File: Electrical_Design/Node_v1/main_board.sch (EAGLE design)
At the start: 23 parts, among them IC1 TP4056, IC2 REG1117

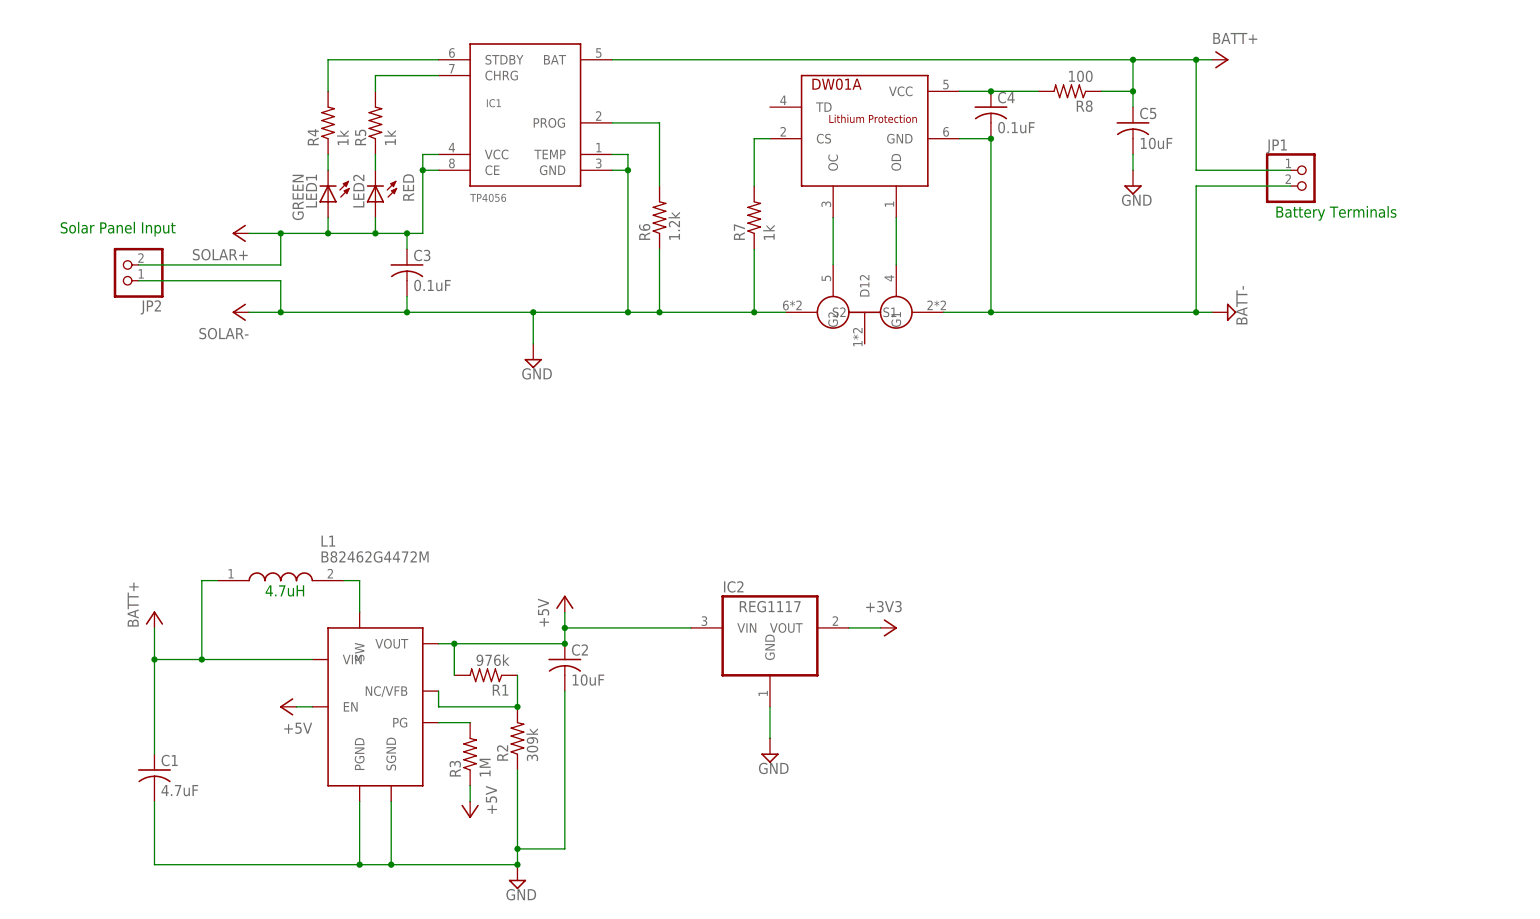
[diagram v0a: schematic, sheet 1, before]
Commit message: Adds current sensor to power page -- Adds microcontroller page
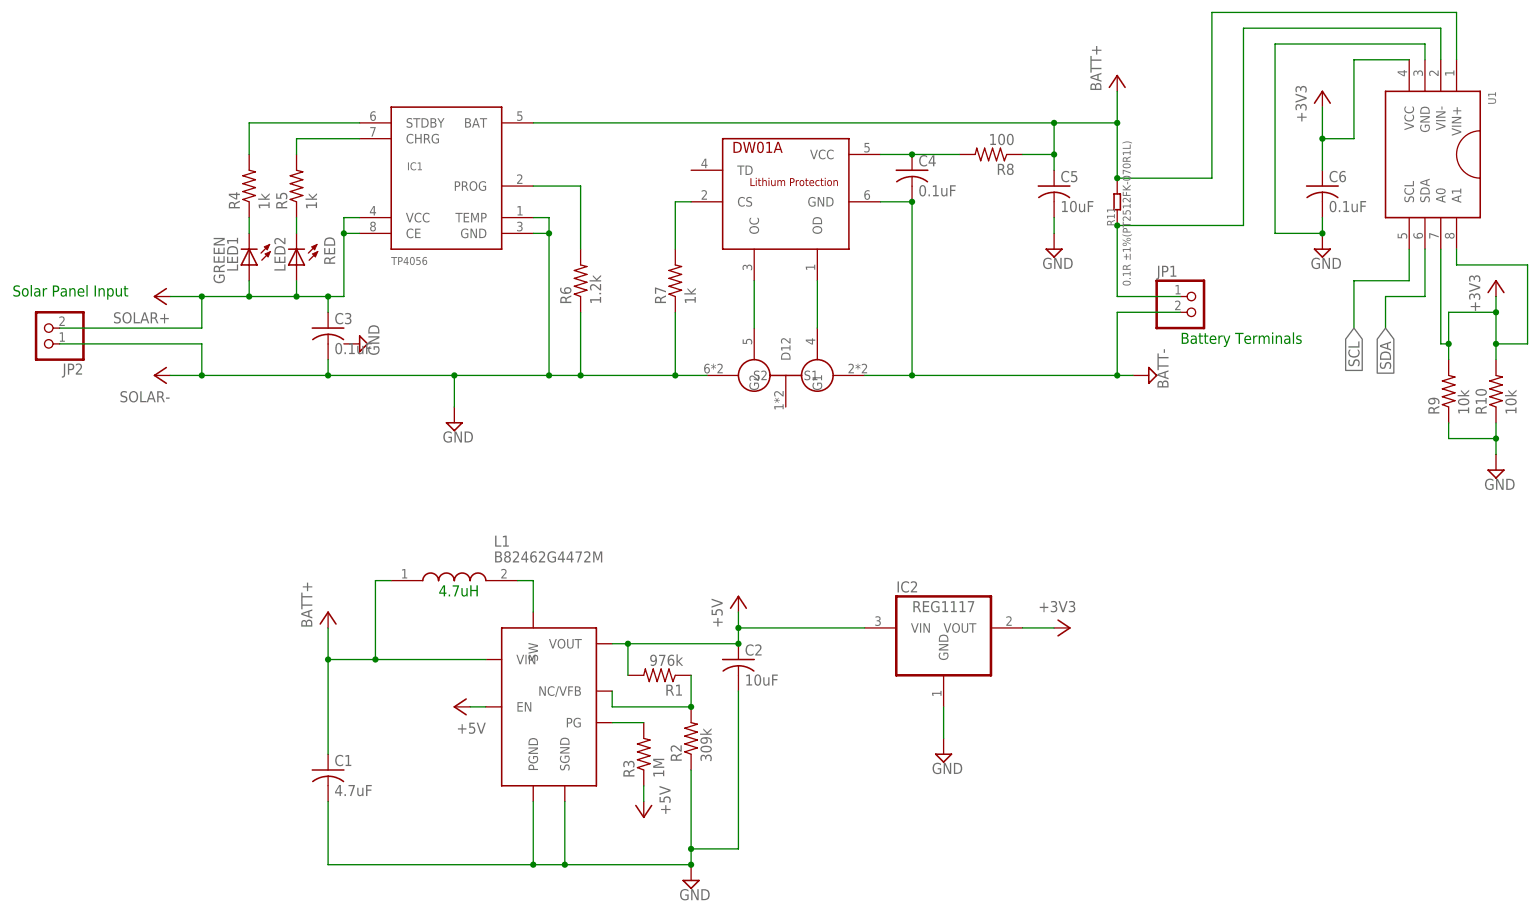
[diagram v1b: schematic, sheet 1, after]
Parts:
- added C6: 0.1uF, adafruit:C-USC1206
- added JP3: (no value), pinhead:PINHD-1X8
- added JP4, JP5: (no value), pinhead:PINHD-1X3
- added JP6: (no value), pinhead:PINHD-1X6
- added R10, R14, R9: 10k, adafruit:R-US_R1206
- added R11: 0.1R ±1%(PT2512FK-070R1L), RCL_INA219:R-2512
- added R12, R13, R15, R16: 4.7k, adafruit:R-US_R1206
- added S3, S4: 222AMVAAR, SamacSys_Parts:222AMVAAR
- added U1: (no value), IC_INA219:INA219
- added U2: ESP-WROOM-32, SparkFun-RF_ESP:ESP-WROOM-32
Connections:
- new net N$13: JP1.1, R11.1, U1.VIN-
- new net N$14: JP3.8, U2.IO5
- new net N$15: JP3.7, U2.IO23
- new net N$16: JP3.6, U2.IO19
- new net N$17: JP3.5, U2.IO18
- new net N$18: JP6.5, R14.1, S3.NO_1, S3.NO_2, U2.EN
- new net N$19: JP6.2, U2.TXD
- new net N$20: JP6.3, U2.RXD
- new net N$21: JP5.2, U2.SENSOR_VN
- new net N$22: JP6.6, S4.NO_1, S4.NO_2, U2.IO0
- new net N$23: JP4.2, R15.1
- new net N$24: R15.2, R16.2, U2.IO34
- new net SCL: JP3.1, R13.1, U1.SCL, U2.IO22
- new net SDA: JP3.2, R12.1, U1.SDA, U2.IO21
- net +3V3: now also C6.1, JP3.3, JP5.1, R10.2, R12.2, R13.2, R14.2, R9.2, U1.A0, U1.A1, U1.VCC, U2.3V3
- net +5V: now also JP4.1, JP6.1
- net BATT+: now also R11.2, U1.VIN+; no longer JP1.1
- net GND: now also C6.2, JP3.4, JP4.3, JP5.3, JP6.4, R10.1, R16.1, R9.1, S3.COM_1, S3.COM_2, S4.COM_1, S4.COM_2, U1.GND, U2.GND, U2.GND@1, U2.GND@15, U2.GND@38
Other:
- note added: "5V-IN"
- note added: "BOOT Button"
- note added: "CS"
- note added: "Camera"
- note added: "EN"
- note added: "EN Button"
- note added: "GND"
- note added: "IO0 (BOOT)"
- note added: "MISO"
- note added: "MOSI"
- note added: "RX"
- note added: "SCK"
- note added: "SCL"
- note added: "SDA"
- note added: "TX"
- note added: "VCC"
- note added: "Wind Direction"
- note added: "Wind Speed"
- moved on the sheet: C1, C2, C3, C4, C5, IC1, IC2, JP1, JP2, L1, LED1, LED2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

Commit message: Completes schematic layout
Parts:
- added C10: 0.22uF, adafruit:C-USC1206
- added C7, C8: 0.1uF, adafruit:C-USC1206
- added C9: 4.7uF, adafruit:C-USC1206
- added IC3: DS18B20U+, SamacSys_Parts:DS18B20U+
- added JP7: (no value), pinhead:PINHD-1X7
- added R17, R18, R21: 4.7k, adafruit:R-US_R1206
- added R19, R20, R22, R23: 10k, adafruit:R-US_R1206
- added TP1, TP10, TP11, TP12, TP13, TP14, TP15, TP16, TP17, TP18, TP19, TP2, TP20, TP21, TP22, TP23, TP24, TP25, TP26, TP27, TP28, TP29, TP3, TP30, TP4, TP5, TP6, TP7, TP8, TP9: TPPAD1-13, testpad:TPPAD1-13
- added U$4: SPARKFUN_HMC5883LSMD, SparkFun_HMC5883L_Breakout_v12:SPARKFUN_HMC5883LSMD
- added U3: BME280, BME280ComponentLibrary:BME280
- added U4: CCS811, CCS811_Breakout_Temp:CCS811
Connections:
- new net GND1: JP7.4
- new net GPIO17: IC3.DQ, R21.1, U2.IO17
- new net N$25: R17.1, U3.!CS
- new net N$26: R19.1, U4.!RESET!
- new net N$27: C10.1, U$4.SETP
- new net N$28: C10.2, U$4.SETC
- new net N$29: R22.2, U4.!WAKE!
- new net N$30: C9.1, U$4.C1
- new net N$31: TP1.TP, U4.SENSE
- new net N$32: TP2.TP, U4.PWM
- new net N$33: TP3.TP, U4.!INT!
- new net N$34: TP4.TP, U4.AUX
- new net N$35: TP5.TP, U$4.DRDY
- new net N$36: TP7.TP, U$1.TD
- new net N$37: TP6.TP, U$2.D12
- new net N$38: TP28.TP, U2.IO2
- new net N$39: TP27.TP, U2.IO4
- new net N$40: TP26.TP, U2.IO12
- new net N$41: TP25.TP, U2.IO13
- new net N$42: TP24.TP, U2.IO14
- new net N$43: TP23.TP, U2.IO15
- new net N$44: TP22.TP, U2.IO16
- new net N$45: TP21.TP, U2.IO20
- new net N$46: TP20.TP, U2.IO25
- new net N$47: TP19.TP, U2.IO26
- new net N$48: TP18.TP, U2.IO27
- new net N$49: TP17.TP, U2.IO32
- new net N$50: TP16.TP, U2.IO33
- new net N$51: TP15.TP, U2.IO35
- new net N$52: TP14.TP, U2.SHD
- new net N$53: TP13.TP, U2.SWP
- new net N$54: TP12.TP, U2.SCS
- new net N$55: TP11.TP, U2.SCK
- new net N$56: TP10.TP, U2.SDO
- new net N$57: TP9.TP, U2.SDI
- new net N$58: TP8.TP, U2.SENSOR_VP
- new net VCC: JP7.1, JP7.2, JP7.3
- net +3V3: now also C7.1, C8.1, IC3.VDD, JP7.6, R17.2, R18.1, R19.2, R20.1, R21.2, R23.1, U$4.S1, U$4.VDD, U$4.VDDIO, U3.VDD, U3.VDDIO, U4.VDD
- net +5V: now also JP7.5
- net GND: now also C7.2, C8.2, C9.2, IC3.GND, JP7.7, R18.2, R20.2, R22.1, U$4.GND@1, U$4.GND@2, U3.GND1, U3.GND2, U3.SDO/ADR, U4.ADDR, U4.GND
- net N$22: now also R23.2
- net SCL: now also TP29.TP, U$4.SCL, U3.SCK/SCL, U4.SCL
- net SDA: now also TP30.TP, U$4.SDA, U3.SDI/SDA, U4.SDA
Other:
- note added: "Optional - I2C Address Selector"
- note added: "Power Test Point"
- moved on the sheet: JP3, JP4, JP5, JP6, R12, R13, R14, R15, R16, S3, S4, U2

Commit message: Begins main board layout
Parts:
- added JP8, JP9: (no value), pinhead:PINHD-1X5
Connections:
- net +3V3: now also JP8.2, JP9.2
- net GND: now also JP8.1, JP9.1
- net GPIO17: now also JP8.5, JP9.5
- net SCL: now also JP8.4, JP9.4
- net SDA: now also JP8.3, JP9.3
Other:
- moved on the sheet: IC3, R21

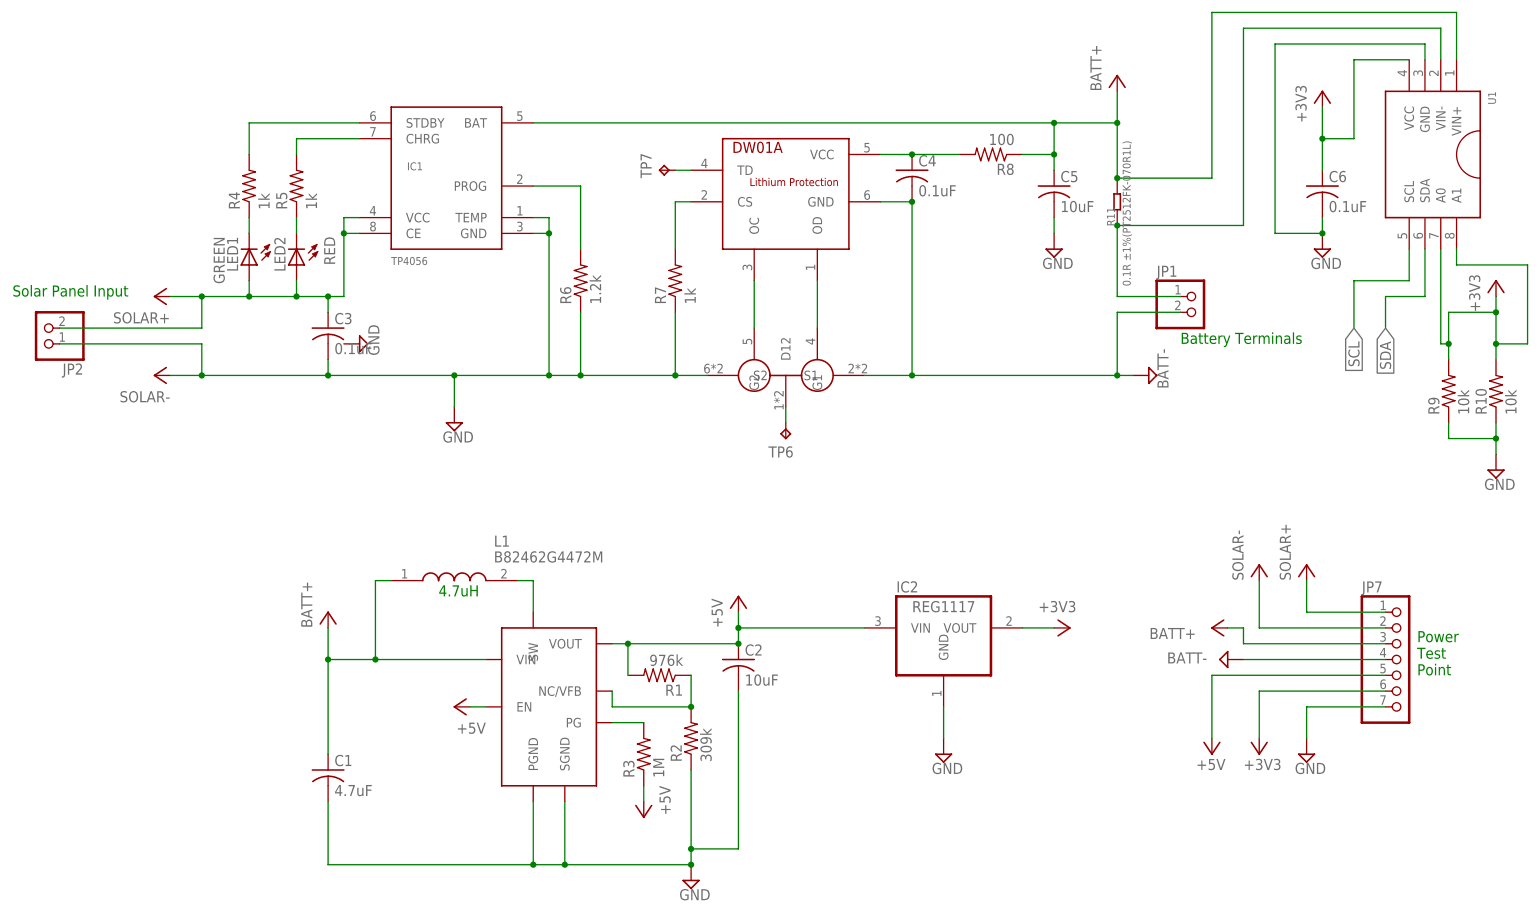
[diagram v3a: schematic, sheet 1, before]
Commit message: Completes main board layout -- outstanding - isolate planes from divider line - remove planes from under esp antenna - generatre drc report
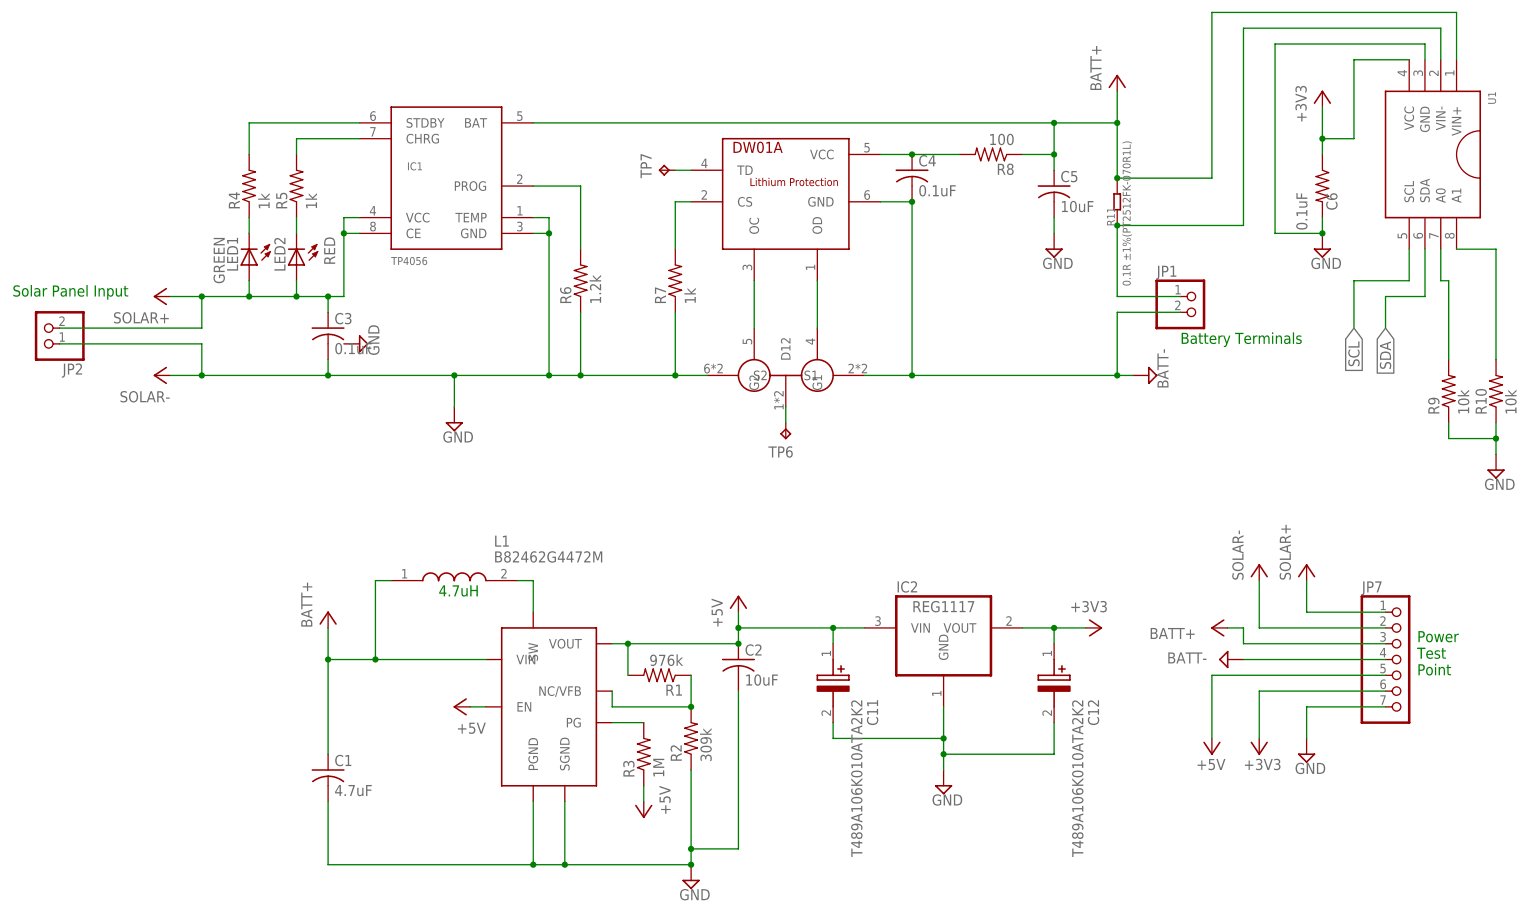
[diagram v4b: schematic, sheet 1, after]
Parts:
- added C11, C12: T489A106K010ATA2K2, SamacSys_Parts:T489A106K010ATA2K2
- C6: device adafruit:C-USC1206 -> adafruit:R-US_R0402
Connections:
- removed net GND1: JP7.4
- removed net VCC: JP7.1, JP7.2, JP7.3
- new net N$60: R9.2, U1.A0
- new net N$61: R10.2, U1.A1
- new net SOLAR-: JP7.2
- net +3V3: now also C12.+; no longer R10.2, R9.2, U1.A0, U1.A1
- net +5V: now also C11.+
- net BATT+: now also JP7.3
- net BATT-: now also JP7.4
- net GND: now also C11.-, C12.-
- net SOLAR+: now also JP7.1

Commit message: Updates Schematics - adds BOM
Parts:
- C1, C9: MF (none) -> MURATA; MPN (none) -> GRM188R61E475KE11D; OC_NEWARK (none) -> 03AC2666
- C10: MF (none) -> TDK; MPN (none) -> C1005X7R1V224K050BE; OC_NEWARK (none) -> 71AH3221
- C11, C12: MF (none) -> KEMET; MPN (none) -> T489A106K010ATA2K2; OC_NEWARK (none) -> 82AH9186
- C2, C5: MF (none) -> MURATA; MPN (none) -> GRM188C80G106ME47D; OC_NEWARK (none) -> 65AH7093
- C3, C4, C6, C7, C8: MF (none) -> KEMET; MPN (none) -> C0805C104M5RACAUTO; OC_NEWARK (none) -> 92AH4371
- IC1, IC2, JP1, JP2, JP7, JP8, JP9, S3, S4, TP1, TP10, TP11, TP12, TP13, TP14, TP15, TP16, TP17, TP18, TP19, TP2, TP20, TP21, TP22, TP23, TP24, TP25, TP26, TP27, TP28, TP29, TP3, TP30, TP4, TP5, TP6, TP7, TP8, TP9, U$1, U$2, U$4, U2: OC_NEWARK (none) -> unknown
- IC3: MF (none) -> MAXIM INTEGRATED / ANALOG DEVICES; MPN (none) -> DS18B20U+T&R; OC_NEWARK (none) -> 73Y1392
- JP3: MF (none) -> L-COM; MPN (none) -> PP5P-08BSS-155N; OC_NEWARK (none) -> 23AK8353
- JP4, JP5: MF (none) -> APEM; MPN (none) -> 1X03; OC_NEWARK (none) -> 06AC4491
- JP6: MF (none) -> APEM; MPN (none) -> 1X06; OC_NEWARK (none) -> 06AC4492
- L1: MF (none) -> EPCOS; MPN (none) -> B82462G4472M000; OC_NEWARK (none) -> 92AH4102
- LED1: MF (none) -> BROADCOM; MPN (none) -> HSMG-C170; OC_NEWARK (none) -> 40K0121
- LED2: MF (none) -> ROHM; MPN (none) -> SML-S13RTT86; OC_NEWARK (none) -> 96Y9625
- R1: MF (none) -> VISHAY; MPN (none) -> CRCW0402976KFKED; OC_NEWARK (none) -> 24W2533
- R10, R14, R19, R20, R22, R23, R9: MF (none) -> YAGEO; MPN (none) -> RT0603BRB0710KL; OC_NEWARK (none) -> 82AH8869
- R11: MF (none) -> YAGEO; MPN (none) -> PT2512FK-070R1L; OC_NEWARK (none) -> 82AH7716
- R12, R13, R15, R16, R17, R18, R21: MF (none) -> MULTICOMP PRO; MPN (none) -> MP000527; OC_NEWARK (none) -> 54AH6417
- R2: MF (none) -> PANASONIC; MPN (none) -> ERJPA3F3093V; OC_NEWARK (none) -> 85Y6391
- R3: MF (none) -> MULTICOMP PRO; MPN (none) -> MCHVR02JTEY1004; OC_NEWARK (none) -> 47AC0009
- R4, R5, R7: MF (none) -> VISHAY; MPN (none) -> MCT06030D1001BP500; OC_NEWARK (none) -> 96Y9448
- R6: MF (none) -> YAGEO; MPN (none) -> RT0603DRE071K2L; OC_NEWARK (none) -> 82AH8972
- R8: MF (none) -> DIODES INC.; MPN (none) -> ZSR1000GTA; OC_NEWARK (none) -> 76AH6132
- U$3: MF (none) -> MICROCHIP; MPN (none) -> MCP1642B-ADJI/MS; OC_NEWARK (none) -> 29Y7746
- U1: MF (none) -> MAXIM INTEGRATED / ANALOG DEVICES; MPN (none) -> MAX6369KA+T; OC_NEWARK (none) -> 81Y9547
- U3: MF (none) -> ADAFRUIT; MPN (none) -> 2652; OC_NEWARK (none) -> 77Y5291
- U4: MF (none) -> ADAFRUIT; MPN (none) -> 3566; OC_NEWARK (none) -> 48AC8695
